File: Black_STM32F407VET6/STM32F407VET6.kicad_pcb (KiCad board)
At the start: 2 copper layers, 99 parts, among them J1 T0, J10 - HotBed +, J11 Heater0, J12 X-, J13 Y-, J14 Z-, J15 Z+, J16 USB_B, J17 LeftSpi, J18 EXTRAPINS, J19 12Vinput, J2 T1, J20 5VOut, J23 EXP2, J24 LCD2004, J25 Bottom, J26 Right, J28 LIGHTS, J29 Z, J3 TB, J30 Z, J38 X, J39 Y, J4 TC, J41 E0, J43 Heater1, J44 COM, J47 I2C, J48 SPI, J49 SPI, J5 + VIN -, J50 SDIO, J51 Servo, J52 Servo, J53 PowerSelect, J54 Power, J55 PD11, J56 Power, J6 Fan3, J7 Fan2, J8 Fan1, J9 Fan0, Q1 BCX70, Q10 BCX70, Q11 BCX70, Q12 IRLR8726PBF, Q13 IRLR8726PBF, Q14 IRLR8726PBF, Q2 BCX70, Q3 BCX70, Q4 IRLML0030TRPBF, Q5 BCX70, Q6 IRLML0030TRPBF, Q7 IRLML0030TRPBF, Q8 IRLML0030TRPBF, Q9 BCX70, SW1 Boot0, U1 LeftAnalog, U2 Left5V, U3 BuckConvertor, U5 AT24CS01-SSHM

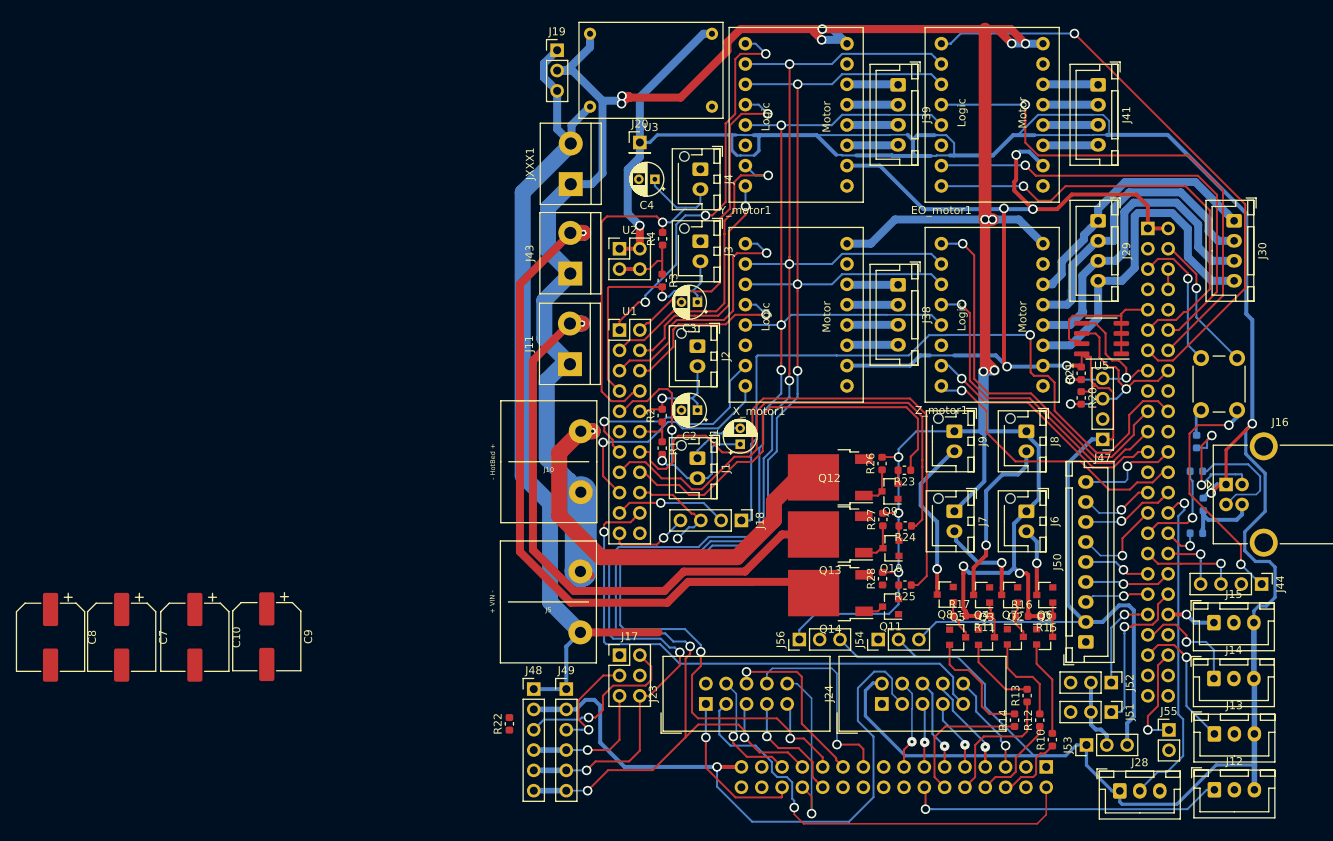
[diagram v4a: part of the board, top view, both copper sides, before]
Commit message: Flipped back resistors to the front
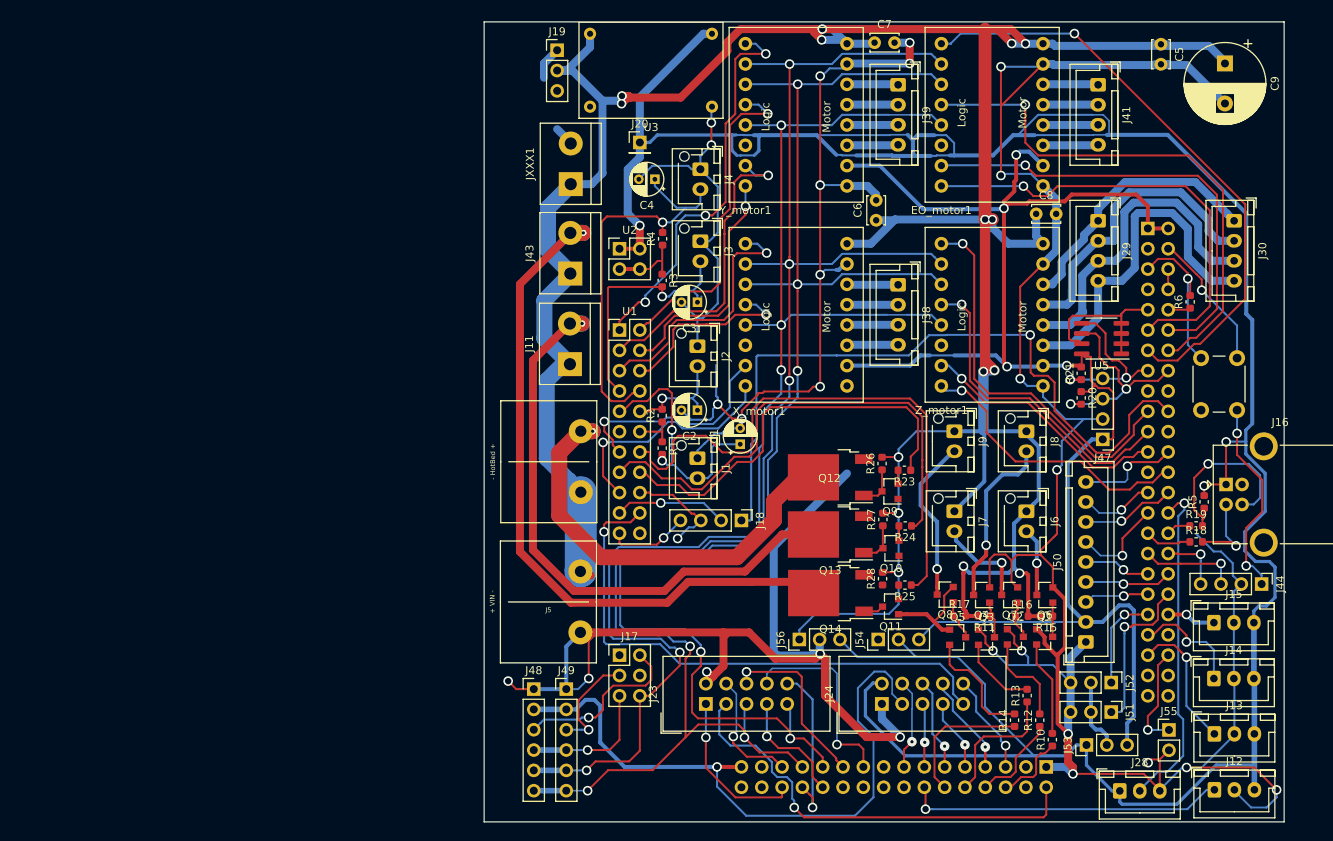
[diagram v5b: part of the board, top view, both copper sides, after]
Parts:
- removed C10: 100uF, Capacitor_SMD:CP_Elec_8x6.9
- removed R22: 4K7, Resistor_SMD:R_0603_1608Metric
- added C5: C 100nF, Capacitor_THT:C_Disc_D3.4mm_W2.1mm_P2.50mm, F.Cu at (189.6, 60.8)
- added C6: C 100nF, Capacitor_THT:C_Disc_D3.4mm_W2.1mm_P2.50mm, F.Cu at (154.0, 82.8)
- C7, C8: value 100uF -> C 100nF; footprint Capacitor_SMD:CP_Elec_8x6.9 -> Capacitor_THT:C_Disc_D3.4mm_W2.1mm_P2.50mm
- C9: value 100uF -> CP 470uF 50V; footprint Capacitor_SMD:CP_Elec_8x6.9 -> Capacitor_THT:CP_Radial_D10.0mm_P5.00mm
- R18, R19, R5, R6: moved to F.Cu
- moved C9 139.6 mm to (197.6, 63.2)
- moved C8 134.1 mm to (174.0, 82.0), turned to 0 degrees
- moved C7 119.9 mm to (153.8, 60.6), turned to 0 degrees
- moved R6 17.5 mm to (193.2, 93.0)
- moved R18 8.83 mm to (194.0, 123.0)
- moved R19 0.92 mm to (194.0, 121.0)
- moved R5 0.33 mm to (195.0, 118.0)
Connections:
- U1 pad 11: GND -> Net-(U1-Pad11)
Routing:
- net GND: track 154.2 -> 599.4 mm, vias 2 -> 26
- net 12V: track 354.9 -> 391.0 mm
- net Net-(J16-Pad3): track 9.47 -> 22.8 mm, vias 0 -> 1
- net USB_DM: track 12.3 -> 5.86 mm, vias 1 -> 0
- net Net-(J26-Pad5): track 25.7 -> 19.8 mm
- net 3V3: track 344.0 -> 338.7 mm, vias 9 -> 8
- net Net-(J16-Pad2): track 14.9 -> 10.1 mm, vias 0 -> 1
- net 5V: track 355.2 -> 352.1 mm
- net USB_DP: track 4.97 -> 3.09 mm, vias 1 -> 0
- net MISO: track 193.6 -> 192.2 mm
- net E0_Step: track 56.2 -> 57.6 mm
- net Reset: track 56.8 -> 55.7 mm
- net E0_CS: track 65.3 -> 66.4 mm
- net E0_En: track 74.3 -> 75.1 mm
- net E0_Dir: track 56.1 -> 56.8 mm
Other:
- board outline added: 100 x 100 mm

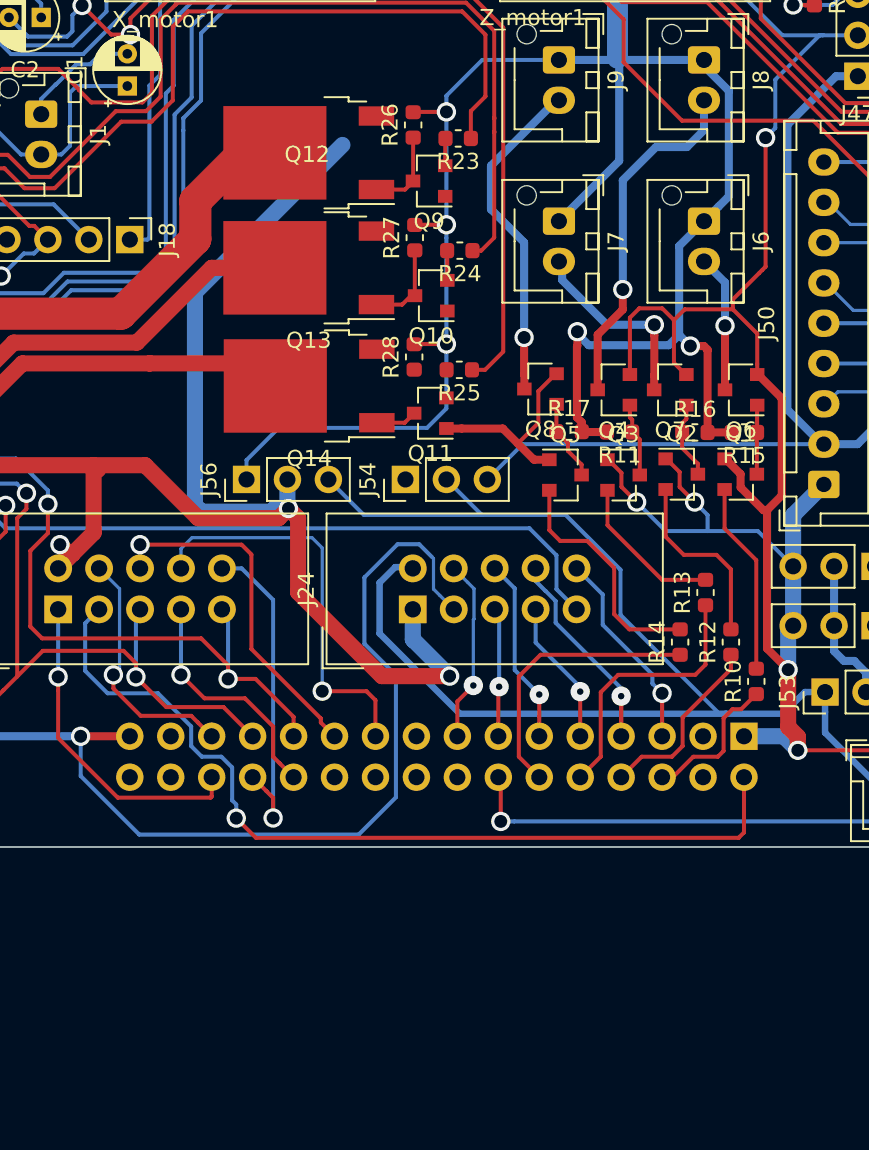
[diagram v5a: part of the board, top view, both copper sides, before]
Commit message: Added comparators to drive the mosfets.
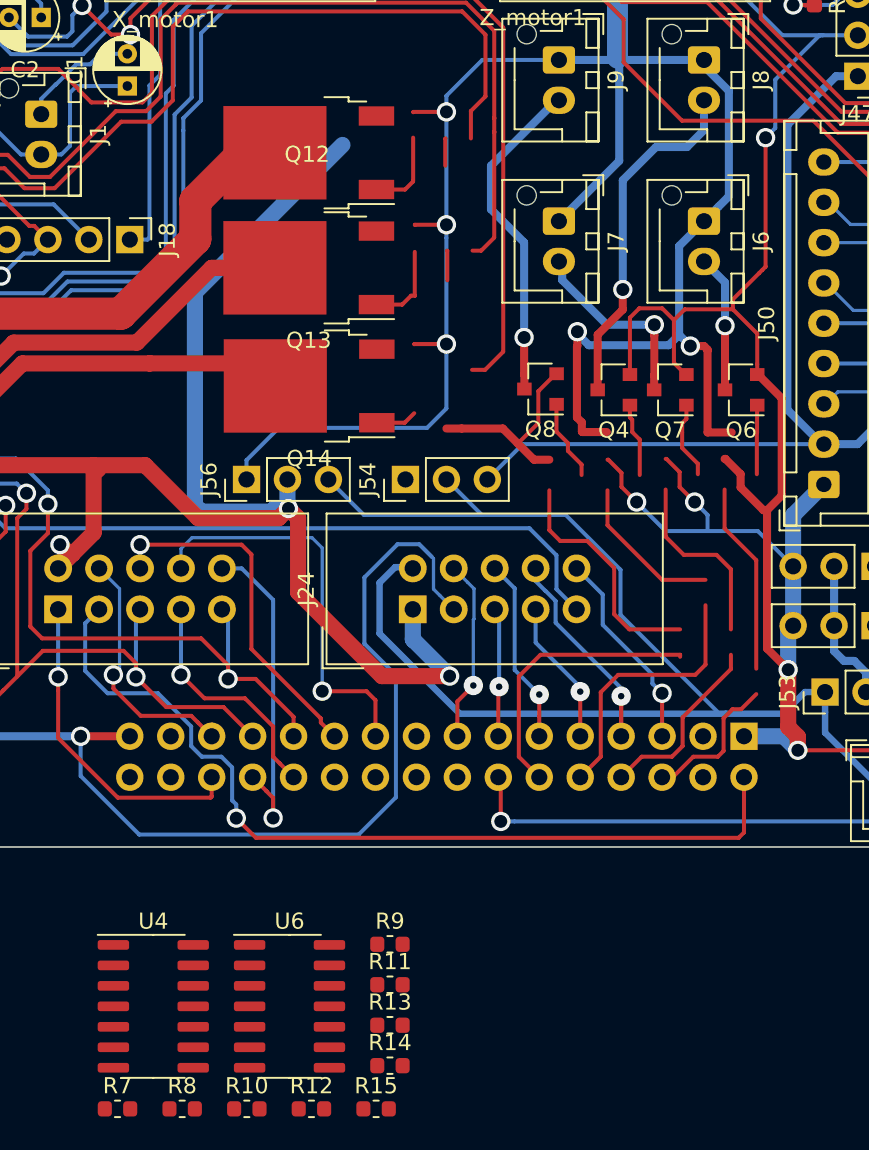
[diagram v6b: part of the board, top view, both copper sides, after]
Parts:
- removed Q1, Q10, Q11, Q2, Q3, Q5, Q9: BCX70, Package_TO_SOT_SMD:SOT-23
- removed R16, R17, R26, R27, R28: 10K, Resistor_SMD:R_0603_1608Metric
- removed R23, R24, R25: 100K, Resistor_SMD:R_0603_1608Metric
- added R7: 10K, Resistor_SMD:R_0603_1608Metric, F.Cu at (136.4, 174.2)
- added R8: 10K, Resistor_SMD:R_0603_1608Metric, F.Cu at (140.4, 174.2)
- added R9: 15K, Resistor_SMD:R_0603_1608Metric, F.Cu at (153.3, 164.0)
- added U4: LM2901, Package_SO:SOIC-14_3.9x8.7mm_P1.27mm, F.Cu at (138.6, 167.9)
- added U6: LM2901, Package_SO:SOIC-14_3.9x8.7mm_P1.27mm, F.Cu at (147.1, 167.9)
- R10, R12, R13, R14: value 100K -> 15K
- R11, R15: value 10K -> 15K
- moved R15 47.8 mm to (152.4, 174.2), turned to 0 degrees
- moved R10 41.3 mm to (144.4, 174.2), turned to 0 degrees
- moved R12 38.9 mm to (148.4, 174.2), turned to 0 degrees
- moved R11 37.1 mm to (153.3, 166.5), turned to 0 degrees
- moved R13 33.2 mm to (153.3, 169.1), turned to 0 degrees
- moved R14 31.8 mm to (153.3, 171.6), turned to 0 degrees
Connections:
- Q13 pad 1: Net-(Q10-Pad3) -> Net-(Q13-Pad1)
- Q14 pad 1: Net-(Q11-Pad3) -> Net-(Q14-Pad1)
- Q6 pad 1: Net-(Q1-Pad3) -> Net-(Q6-Pad1)
- Q7 pad 1: Net-(Q2-Pad3) -> Net-(Q7-Pad1)
- Q8 pad 1: Net-(Q5-Pad3) -> Net-(Q8-Pad1)
- R10 pad 1: Fan3 -> Net-(Q7-Pad1)
- R10 pad 2: Net-(Q1-Pad2) -> 12V
- R12 pad 1: Fan2 -> Net-(Q8-Pad1)
- R12 pad 2: Net-(Q2-Pad2) -> 12V
- R13 pad 1: Fan1 -> Net-(Q12-Pad1)
- R13 pad 2: Net-(Q3-Pad2) -> 12V
- R14 pad 1: Fan0 -> Net-(Q13-Pad1)
- R14 pad 2: Net-(Q5-Pad2) -> 12V
- R15 pad 1: Net-(Q1-Pad3) -> Net-(Q14-Pad1)
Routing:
- net Net-(Q13-Pad1): track 0.00 -> 5.35 mm
- net Net-(Q10-Pad3): track 5.35 -> 0.00 mm
- net Net-(Q8-Pad1): track 0.00 -> 5.03 mm
- net Net-(Q5-Pad3): track 5.03 -> 0.00 mm
- net Net-(Q7-Pad1): track 0.00 -> 4.80 mm
- net Net-(Q2-Pad3): track 4.80 -> 0.00 mm
- net Net-(Q6-Pad1): track 0.00 -> 4.29 mm
- net Net-(Q1-Pad3): track 4.29 -> 0.00 mm
- net Net-(Q14-Pad1): track 0.00 -> 2.56 mm
- net Net-(Q11-Pad3): track 2.56 -> 0.00 mm

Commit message: Board layout with the opamps
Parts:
- Q4, Q6, Q7, Q8, R10, R11, R12, R9, U6: moved to B.Cu
- moved U6 57.5 mm to (150.4, 110.5)
- moved R13 52.0 mm to (156.0, 117.1)
- moved R10 50.5 mm to (165.9, 128.5), turned to 270 degrees
- moved R7 49.8 mm to (172.0, 139.4), turned to 90 degrees
- moved U4 49.4 mm to (172.7, 132.1)
- moved R12 47.6 mm to (161.5, 128.5), turned to 270 degrees
- moved R14 47.2 mm to (156.0, 124.5)
- moved R8 44.6 mm to (172.0, 142.7), turned to 90 degrees
- moved R15 42.6 mm to (156.0, 131.8)
- moved R11 41.5 mm to (169.9, 128.5), turned to 270 degrees
- moved R9 41.0 mm to (174.0, 128.7), turned to 270 degrees
- moved Q7 5.84 mm to (166.9, 125.2), turned to 0 degrees
- moved Q4 5.80 mm to (170.9, 125.2), turned to 0 degrees
- moved Q6 4.42 mm to (175.1, 125.2), turned to 0 degrees
- moved Q8 4.37 mm to (162.6, 125.2), turned to 0 degrees
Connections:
- J25 pad 10: Fan1 -> Fan2
- J25 pad 12: Fan0 -> Fan3
- J25 pad 6: Fan3 -> Fan1
- J25 pad 8: Fan2 -> Fan0
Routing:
- net Vref: track 0.00 -> 75.6 mm, vias 0 -> 1
- net GND: track 599.4 -> 637.9 mm, vias 26 -> 30
- net 12V: track 391.0 -> 424.2 mm
- net Heater0: track 62.3 -> 35.6 mm, vias 0 -> 1
- net 3V3: track 338.7 -> 364.0 mm, vias 8 -> 10
- net Net-(Q14-Pad1): track 2.56 -> 25.5 mm, vias 0 -> 1
- net Heater1: track 70.5 -> 48.7 mm, vias 0 -> 1
- net HotBed: track 50.6 -> 33.1 mm, vias 0 -> 1
- net Fan3: track 9.17 -> 24.1 mm
- net Net-(Q5-Pad2): track 14.8 -> 0.00 mm
- net Net-(Q13-Pad1): track 5.35 -> 18.6 mm, vias 0 -> 1
- net Net-(Q8-Pad1): track 5.03 -> 18.0 mm, vias 0 -> 1
- net Net-(Q1-Pad2): track 11.9 -> 0.00 mm
- net Net-(Q2-Pad2): track 11.5 -> 0.00 mm
- net Fan1: track 16.7 -> 28.0 mm
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
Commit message: Added fill zones
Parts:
- moved C1 188.9 mm to (-18.0, 2.79)
- moved C2 188.9 mm to (-23.3, -1.46)
- moved C3 188.9 mm to (-23.3, -15.0)
- moved C4 188.9 mm to (-28.7, -30.3)
- moved C5 188.9 mm to (34.6, -47.2)
- moved C6 188.9 mm to (-1.00, -25.2)
- moved C7 188.9 mm to (-1.20, -47.4)
- moved C8 188.9 mm to (19.0, -26.0)
- moved C9 188.9 mm to (42.6, -44.8)
- moved EO_motor1 188.9 mm to (5.12, -27.5)
- moved J1 188.9 mm to (-23.3, 4.54)
- moved J10 188.9 mm to (-41.9, 4.98)
- moved J11 188.9 mm to (-39.3, -7.21)
- moved J12 188.9 mm to (41.3, 46.0)
- moved J13 188.9 mm to (41.3, 39.0)
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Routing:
- net GND: track 637.9 -> 642.9 mm
- added copper zone on B.Cu, net GND
- added copper zone on F.Cu, net GND
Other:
- rule via_min_size: 0.4 -> 1.2
